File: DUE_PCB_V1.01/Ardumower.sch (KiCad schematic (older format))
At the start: 61 parts, among them J1 I2C_1, J10 Bumper Left, J11 Bumper Right, J12 P_Left, J13 P_Right, J14 Sonar_R, J15 Sonar_C, J16 Sonar_L, J17 US1, J18 US2, J19 US3, J2 I2C_2, J20 Button, J21 5V IN, J22 Remote, J23 PCB_2, J24 3.3V IN, J25 TX0/RX0, J26 TX1/RX1, J27 TX2/RX2, J28 GPS_TX/GPS_RX, J3 I2C_3, J4 DS3231 RTC, J5 9V IN, J6 Drop_Left, J7 Drop_Right, J8 Tilt, J9 Rain

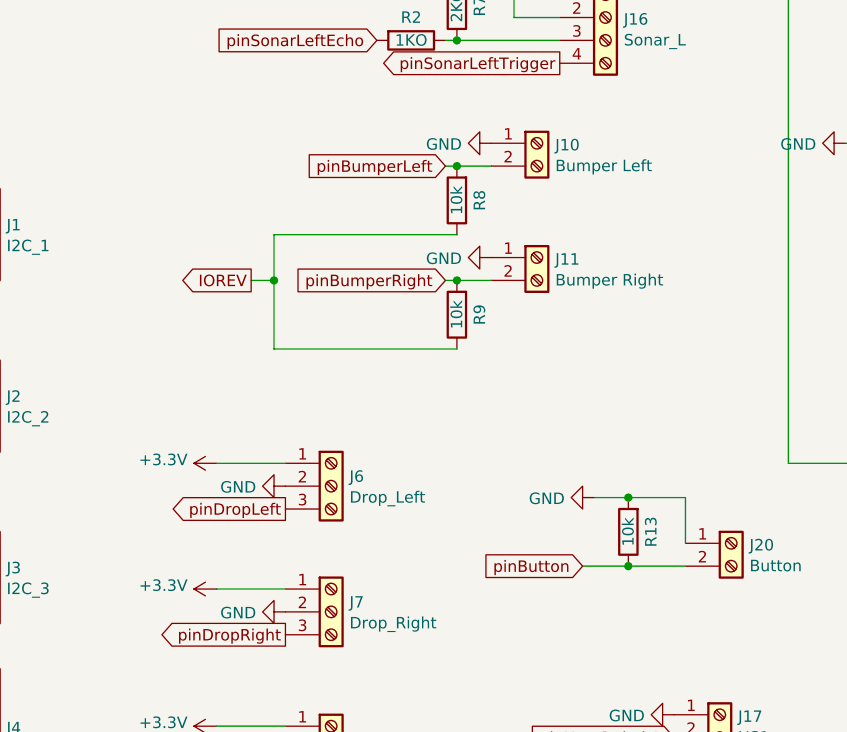
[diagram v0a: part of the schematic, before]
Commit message: Remove Resistors
Remove R8, R9 and R13
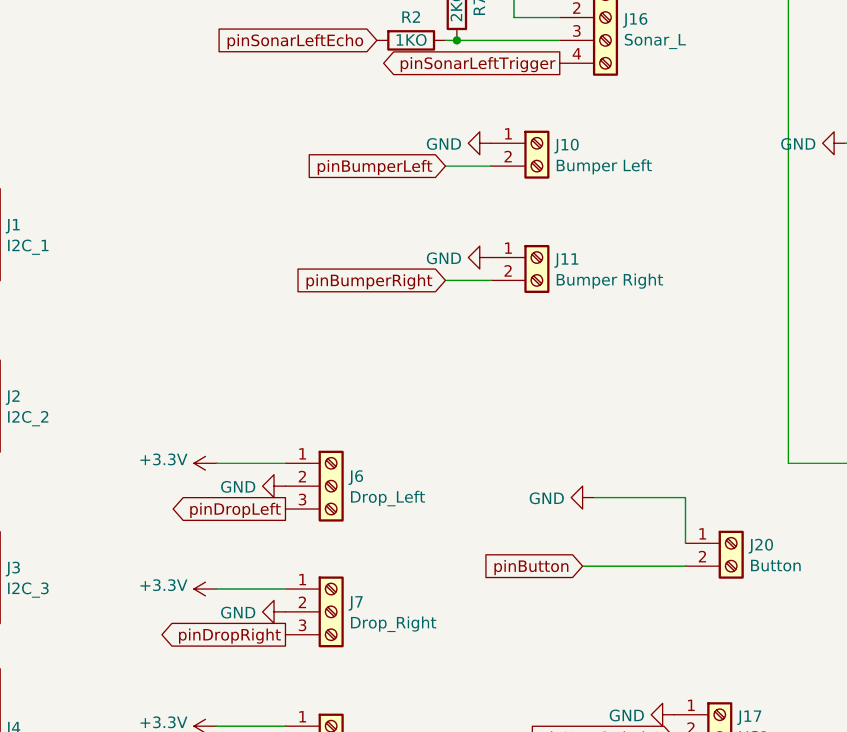
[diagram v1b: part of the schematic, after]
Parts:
- removed R13, R8, R9: 10k, Resistor_THT:R_Axial_DIN0207_L6.3mm_D2.5mm_P2.54mm_Vertical, symbol Device:R
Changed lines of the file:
@@
 ReservePinA10
 Wire Wire Line
-	2050 5000 2100 5000
-$Comp
-L Device:R R9
-U 1 1 6095136A
-P 2100 5150
-F 0 "R9" V 2000 5150 50  0000 C CNN
-F 1 "10k" V 2100 5150 50  0000 C CNN
-F 2 "Resistor_THT:R_Axial_DIN0207_L6.3mm_D2.5mm_P2.54mm_Vertical" V 2030 5150 50  0001 C CNN
-F 3 "~" H 2100 5150 50  0001 C CNN
-	1    2100 5150
-	-1   0    0    1
-$EndComp
-Connection ~ 2100 5000
-Wire Wire Line
-	2100 5000 2250 5000
-$Comp
-L Device:R R8
-U 1 1 6095AC18
-P 2100 4650
-F 0 "R8" V 2000 4650 50  0000 C CNN
-F 1 "10k" V 2100 4650 50  0000 C CNN
-F 2 "Resistor_THT:R_Axial_DIN0207_L6.3mm_D2.5mm_P2.54mm_Vertical" V 2030 4650 50  0001 C CNN
-F 3 "~" H 2100 4650 50  0001 C CNN
-	1    2100 4650
-	-1   0    0    1
-$EndComp
-Wire Wire Line
-	2050 4500 2100 4500
-Connection ~ 2100 4500
-Wire Wire Line
-	2100 4500 2250 4500
-Wire Wire Line
-	2100 4800 1300 4800
-Wire Wire Line
-	1300 4800 1300 5000
-Wire Wire Line
-	1300 5300 2100 5300
-Text GLabel 1200 5000 0    50   Output ~ 0
-IOREV
-Wire Wire Line
-	1200 5000 1300 5000
-Connection ~ 1300 5000
-Wire Wire Line
-	1300 5000 1300 5300
-Wire Wire Line
 	900  850  3550 850
-$Comp
-L Device:R R13
-U 1 1 60986E74
-P 2850 6100
-F 0 "R13" V 2750 6100 50  0000 C CNN
-F 1 "10k" V 2850 6100 50  0000 C CNN
-F 2 "Resistor_THT:R_Axial_DIN0207_L6.3mm_D2.5mm_P2.54mm_Vertical" V 2780 6100 50  0001 C CNN
-F 3 "~" H 2850 6100 50  0001 C CNN
-	1    2850 6100
-	-1   0    0    1
-$EndComp
-Wire Wire Line
-	2650 6250 2850 6250
-Connection ~ 2850 6250
-Wire Wire Line
-	2850 6250 3100 6250
-Wire Wire Line
-	2850 5950 2700 5950
 Wire Wire Line
 	10350 2400 10200 2400
@@
 $EndComp
 Wire Wire Line
-	2850 5950 3100 5950
-Wire Wire Line
 	3100 5950 3100 6150
-Connection ~ 2850 5950
 $Comp
 L Connector:Screw_Terminal_01x05 J25
@@
 	0    1    1    0
 $EndComp
+Wire Wire Line
+	2050 5000 2250 5000
+Wire Wire Line
+	2050 4500 2250 4500
+Wire Wire Line
+	2650 6250 3100 6250
+Wire Wire Line
+	2700 5950 3100 5950
 $EndSCHEMATC

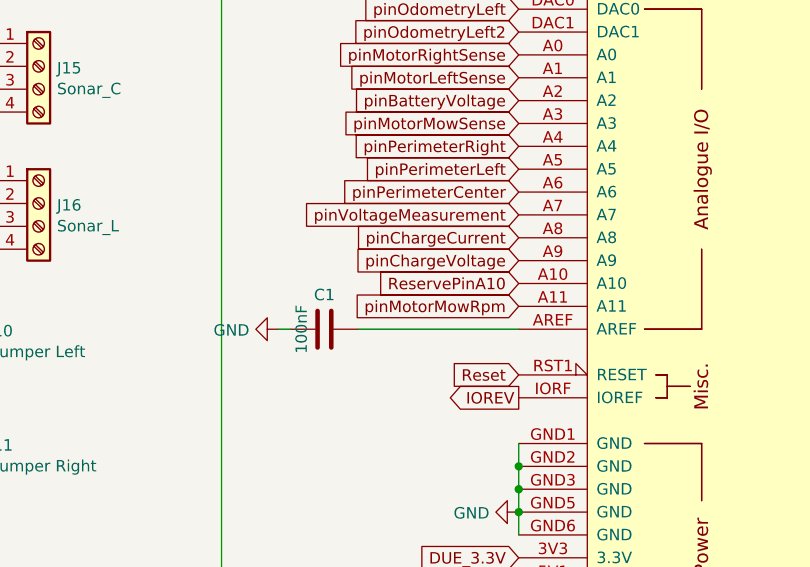
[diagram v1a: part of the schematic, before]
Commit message: Rename Pins
Rename ReservePinA10 to pinMotorLeftSense2
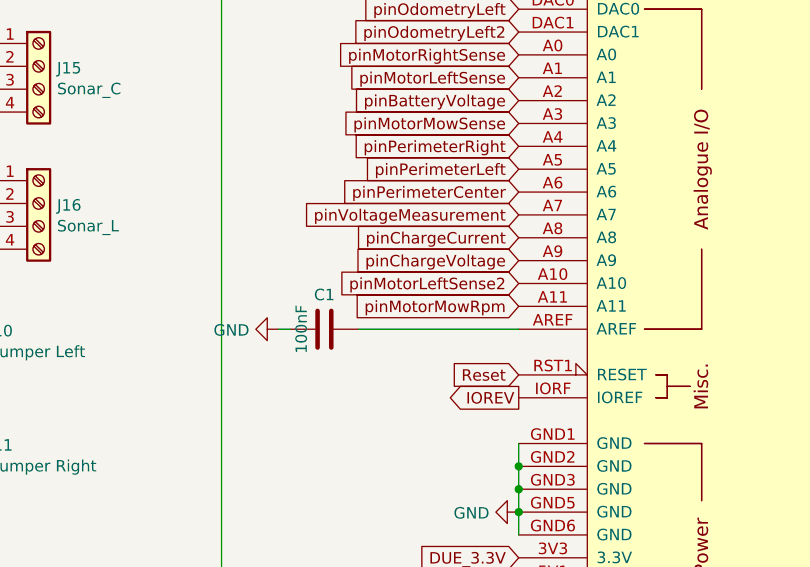
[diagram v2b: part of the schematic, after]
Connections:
- net ReservePinA10: no longer XA1.A10
- new net pinMotorLeftSense2: XA1.A10
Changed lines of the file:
@@
 ReservePinD49
 Text GLabel 4850 4200 0    50   Input ~ 0
-ReservePinA10
+pinMotorLeftSense2
 Text GLabel 9550 1300 0    50   Input ~ 0
 ReservePinA10

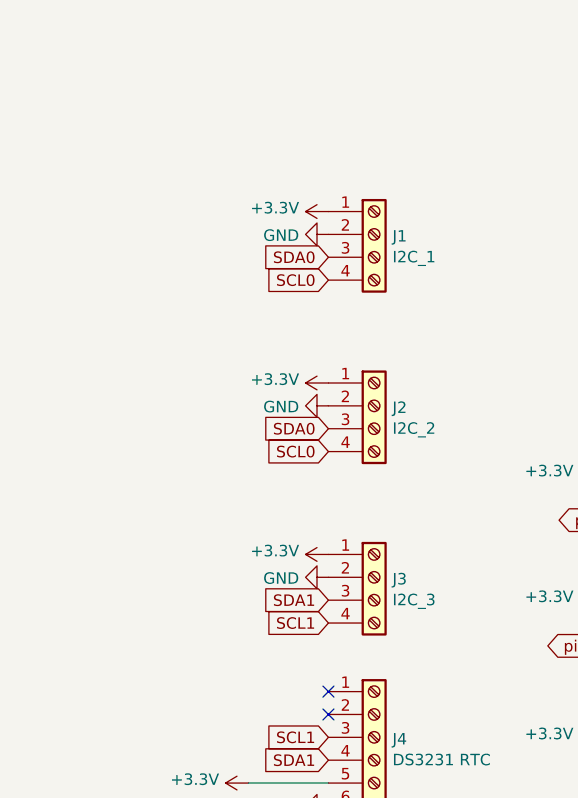
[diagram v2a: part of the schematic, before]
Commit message: Add I2C Pullup
Add i2c Pullup to J1 & J3
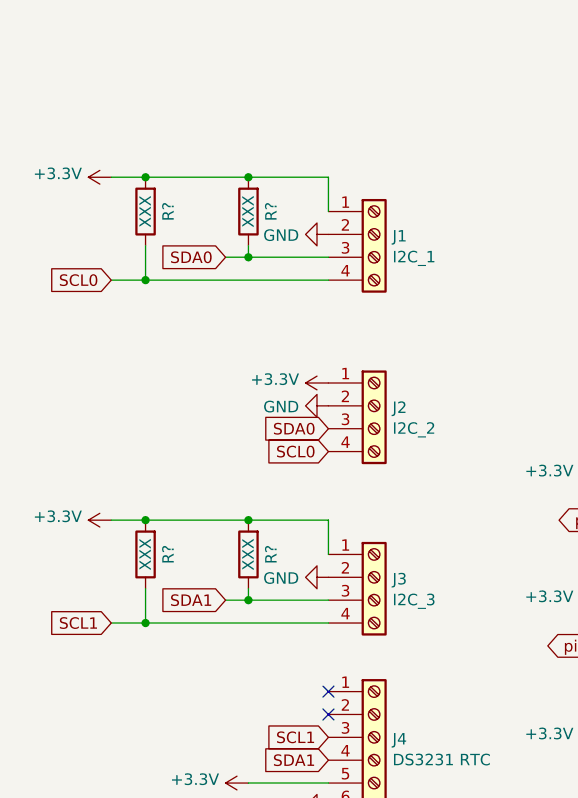
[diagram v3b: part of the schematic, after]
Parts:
- added R? (x4): XXX, Resistor_THT:R_Axial_DIN0207_L6.3mm_D2.5mm_P2.54mm_Vertical, symbol Device:R
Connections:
- net +3V3: now also R?.2, R?.2, R?.2, R?.2
- net SCL0: now also R?.1
- net SCL1: now also R?.1
- net SDA0: now also R?.1
- net SDA1: now also R?.1
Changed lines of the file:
@@
 Text GLabel 4850 2500 0    50   Input ~ 0
 SDA1
-Text GLabel -150 4850 0    50   Input ~ 0
+Text GLabel -600 4850 0    50   Input ~ 0
 SDA0
 Text GLabel -150 5600 0    50   Input ~ 0
 SDA0
-Text GLabel -150 6350 0    50   Input ~ 0
-SDA1
 Text GLabel 4850 2600 0    50   Input ~ 0
 SCL1
-Text GLabel -150 4950 0    50   Input ~ 0
+Text GLabel -1100 4950 0    50   Input ~ 0
 SCL0
 Text GLabel -150 5700 0    50   Input ~ 0
 SCL0
-Text GLabel -150 6450 0    50   Input ~ 0
-SCL1
 $Comp
 L Connector:Screw_Terminal_01x02 J5
@@
 $EndComp
 $Comp
-L power:GND #PWR07
-U 1 1 6097FEEB
-P -150 6250
-F 0 "#PWR07" H -150 6000 50  0001 C CNN
-F 1 "GND" V -145 6122 50  0000 R CNN
-F 2 "" H -150 6250 50  0001 C CNN
-F 3 "" H -150 6250 50  0001 C CNN
-	1    -150 6250
-	0    1    1    0
-$EndComp
-$Comp
 L power:GND #PWR05
 U 1 1 609801E6
@@
 L power:+3.3V #PWR02
 U 1 1 60A55674
-P -150 4650
-F 0 "#PWR02" H -150 4500 50  0001 C CNN
-F 1 "+3.3V" V -135 4778 50  0000 L CNN
-F 2 "" H -150 4650 50  0001 C CNN
-F 3 "" H -150 4650 50  0001 C CNN
-	1    -150 4650
+P -1100 4500
+F 0 "#PWR02" H -1100 4350 50  0001 C CNN
+F 1 "+3.3V" V -1085 4628 50  0000 L CNN
+F 2 "" H -1100 4500 50  0001 C CNN
+F 3 "" H -1100 4500 50  0001 C CNN
+	1    -1100 4500
 	0    -1   -1   0
 $EndComp
@@
 F 3 "" H -150 5400 50  0001 C CNN
 	1    -150 5400
-	0    -1   -1   0
-$EndComp
-$Comp
-L power:+3.3V #PWR06
-U 1 1 60A57F6D
-P -150 6150
-F 0 "#PWR06" H -150 6000 50  0001 C CNN
-F 1 "+3.3V" V -135 6278 50  0000 L CNN
-F 2 "" H -150 6150 50  0001 C CNN
-F 3 "" H -150 6150 50  0001 C CNN
-	1    -150 6150
 	0    -1   -1   0
 $EndComp
@@
 Wire Wire Line
 	2700 5950 3100 5950
+$Comp
+L Device:R R?
+U 1 1 609850CF
+P -950 4650
+F 0 "R?" V -1050 4650 50  0000 C CNN
+F 1 "XXX" V -950 4650 50  0000 C CNN
+F 2 "Resistor_THT:R_Axial_DIN0207_L6.3mm_D2.5mm_P2.54mm_Vertical" V -1020 4650 50  0001 C CNN
+F 3 "~" H -950 4650 50  0001 C CNN
+	1    -950 4650
+	-1   0    0    1
+$EndComp
+$Comp
+L Device:R R?
+U 1 1 6098F377
+P -500 4650
+F 0 "R?" V -600 4650 50  0000 C CNN
+F 1 "XXX" V -500 4650 50  0000 C CNN
+F 2 "Resistor_THT:R_Axial_DIN0207_L6.3mm_D2.5mm_P2.54mm_Vertical" V -570 4650 50  0001 C CNN
+F 3 "~" H -500 4650 50  0001 C CNN
+	1    -500 4650
+	-1   0    0    1
+$EndComp
+Wire Wire Line
+	-1100 4500 -950 4500
+Connection ~ -950 4500
+Wire Wire Line
+	-950 4500 -500 4500
+Wire Wire Line
+	-500 4500 -150 4500
+Wire Wire Line
+	-150 4500 -150 4650
+Connection ~ -500 4500
+Wire Wire Line
+	-600 4850 -500 4850
+Wire Wire Line
+	-500 4800 -500 4850
+Connection ~ -500 4850
+Wire Wire Line
+	-500 4850 -150 4850
+Wire Wire Line
+	-1100 4950 -950 4950
+Wire Wire Line
+	-950 4950 -950 4800
+Wire Wire Line
+	-950 4950 -150 4950
+Connection ~ -950 4950
+Text GLabel -600 6350 0    50   Input ~ 0
+SDA1
+Text GLabel -1100 6450 0    50   Input ~ 0
+SCL1
+$Comp
+L power:GND #PWR?
+U 1 1 609A6BE2
+P -150 6250
+F 0 "#PWR?" H -150 6000 50  0001 C CNN
+F 1 "GND" V -145 6122 50  0000 R CNN
+F 2 "" H -150 6250 50  0001 C CNN
+F 3 "" H -150 6250 50  0001 C CNN
+	1    -150 6250
+	0    1    1    0
+$EndComp
+$Comp
+L power:+3.3V #PWR?
+U 1 1 609A6BEC
+P -1100 6000
+F 0 "#PWR?" H -1100 5850 50  0001 C CNN
+F 1 "+3.3V" V -1085 6128 50  0000 L CNN
+F 2 "" H -1100 6000 50  0001 C CNN
+F 3 "" H -1100 6000 50  0001 C CNN
+	1    -1100 6000
+	0    -1   -1   0
+$EndComp
+$Comp
+L Device:R R?
+U 1 1 609A6BF6
+P -950 6150
+F 0 "R?" V -1050 6150 50  0000 C CNN
+F 1 "XXX" V -950 6150 50  0000 C CNN
+F 2 "Resistor_THT:R_Axial_DIN0207_L6.3mm_D2.5mm_P2.54mm_Vertical" V -1020 6150 50  0001 C CNN
+F 3 "~" H -950 6150 50  0001 C CNN
+	1    -950 6150
+	-1   0    0    1
+$EndComp
+$Comp
+L Device:R R?
+U 1 1 609A6C00
+P -500 6150
+F 0 "R?" V -600 6150 50  0000 C CNN
+F 1 "XXX" V -500 6150 50  0000 C CNN
+F 2 "Resistor_THT:R_Axial_DIN0207_L6.3mm_D2.5mm_P2.54mm_Vertical" V -570 6150 50  0001 C CNN
+F 3 "~" H -500 6150 50  0001 C CNN
+	1    -500 6150
+	-1   0    0    1
+$EndComp
+Wire Wire Line
+	-1100 6000 -950 6000
+Connection ~ -950 6000
+Wire Wire Line
+	-950 6000 -500 6000
+Wire Wire Line
+	-500 6000 -150 6000
+Connection ~ -500 6000
+Wire Wire Line
+	-600 6350 -500 6350
+Wire Wire Line
+	-500 6300 -500 6350
+Connection ~ -500 6350
+Wire Wire Line
+	-500 6350 -150 6350
+Wire Wire Line
+	-1100 6450 -950 6450
+Wire Wire Line
+	-950 6450 -950 6300
+Wire Wire Line
+	-950 6450 -150 6450
+Connection ~ -950 6450
+Wire Wire Line
+	-150 6000 -150 6150
 $EndSCHEMATC

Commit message: Update J30 and J32
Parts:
- gave numbers to parts that had none: 4
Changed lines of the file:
@@
 	2700 5950 3100 5950
 $Comp
-L Device:R R?
+L Device:R R8
 U 1 1 609850CF
 P -950 4650
-F 0 "R?" V -1050 4650 50  0000 C CNN
+F 0 "R8" V -1050 4650 50  0000 C CNN
 F 1 "XXX" V -950 4650 50  0000 C CNN
 F 2 "Resistor_THT:R_Axial_DIN0207_L6.3mm_D2.5mm_P2.54mm_Vertical" V -1020 4650 50  0001 C CNN
@@
 $EndComp
 $Comp
-L Device:R R?
+L Device:R R13
 U 1 1 6098F377
 P -500 4650
-F 0 "R?" V -600 4650 50  0000 C CNN
+F 0 "R13" V -600 4650 50  0000 C CNN
 F 1 "XXX" V -500 4650 50  0000 C CNN
 F 2 "Resistor_THT:R_Axial_DIN0207_L6.3mm_D2.5mm_P2.54mm_Vertical" V -570 4650 50  0001 C CNN
@@
 SCL1
 $Comp
-L power:GND #PWR?
+L power:GND #PWR07
 U 1 1 609A6BE2
 P -150 6250
-F 0 "#PWR?" H -150 6000 50  0001 C CNN
+F 0 "#PWR07" H -150 6000 50  0001 C CNN
 F 1 "GND" V -145 6122 50  0000 R CNN
 F 2 "" H -150 6250 50  0001 C CNN
@@
 $EndComp
 $Comp
-L power:+3.3V #PWR?
+L power:+3.3V #PWR06
 U 1 1 609A6BEC
 P -1100 6000
-F 0 "#PWR?" H -1100 5850 50  0001 C CNN
+F 0 "#PWR06" H -1100 5850 50  0001 C CNN
 F 1 "+3.3V" V -1085 6128 50  0000 L CNN
 F 2 "" H -1100 6000 50  0001 C CNN
@@
 $EndComp
 $Comp
-L Device:R R?
+L Device:R R9
 U 1 1 609A6BF6
 P -950 6150
-F 0 "R?" V -1050 6150 50  0000 C CNN
+F 0 "R9" V -1050 6150 50  0000 C CNN
 F 1 "XXX" V -950 6150 50  0000 C CNN
 F 2 "Resistor_THT:R_Axial_DIN0207_L6.3mm_D2.5mm_P2.54mm_Vertical" V -1020 6150 50  0001 C CNN
@@
 $EndComp
 $Comp
-L Device:R R?
+L Device:R R27
 U 1 1 609A6C00
 P -500 6150
-F 0 "R?" V -600 6150 50  0000 C CNN
+F 0 "R27" V -600 6150 50  0000 C CNN
 F 1 "XXX" V -500 6150 50  0000 C CNN
 F 2 "Resistor_THT:R_Axial_DIN0207_L6.3mm_D2.5mm_P2.54mm_Vertical" V -570 6150 50  0001 C CNN

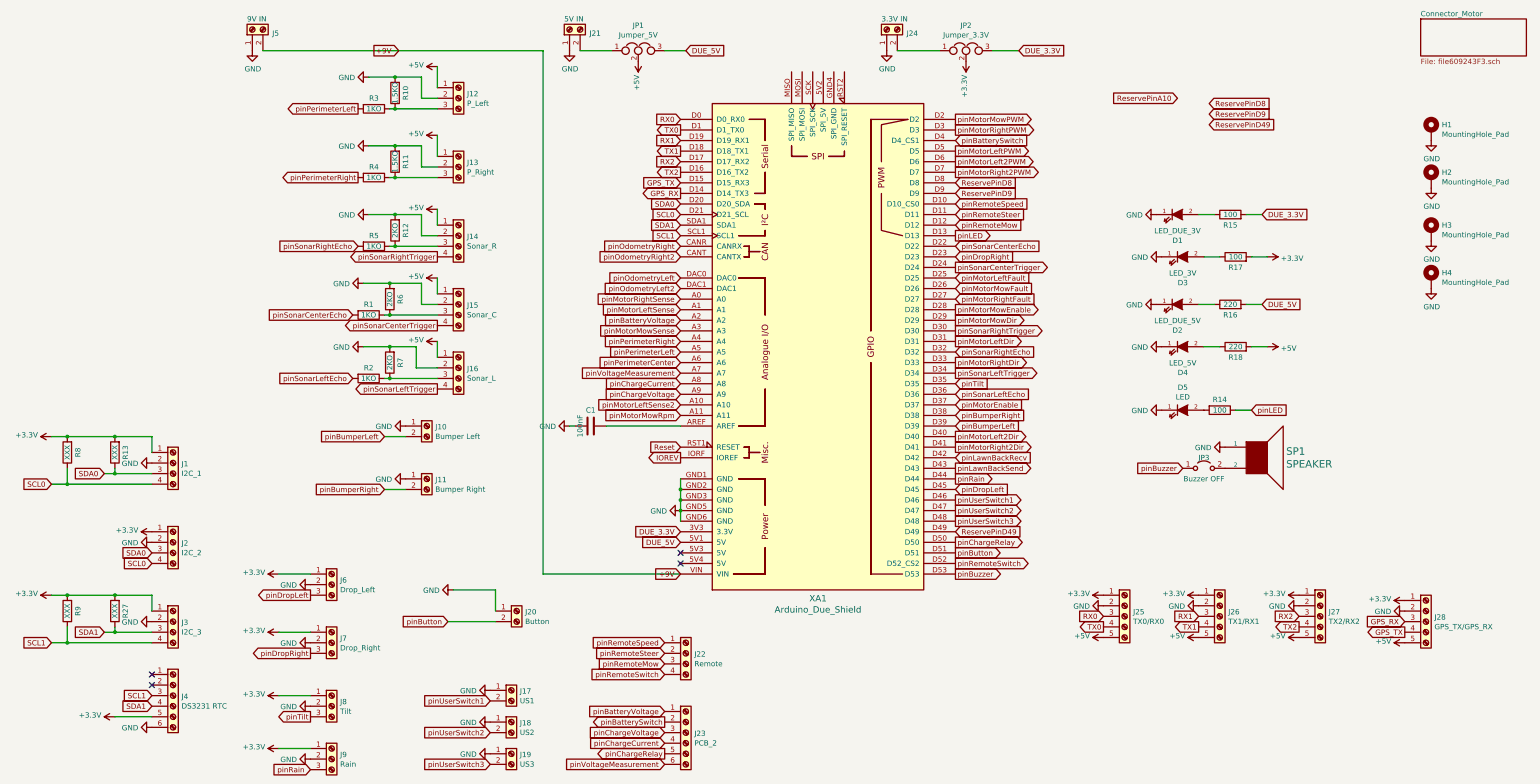
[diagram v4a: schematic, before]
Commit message: Start ro add Bernard changes from 1.02
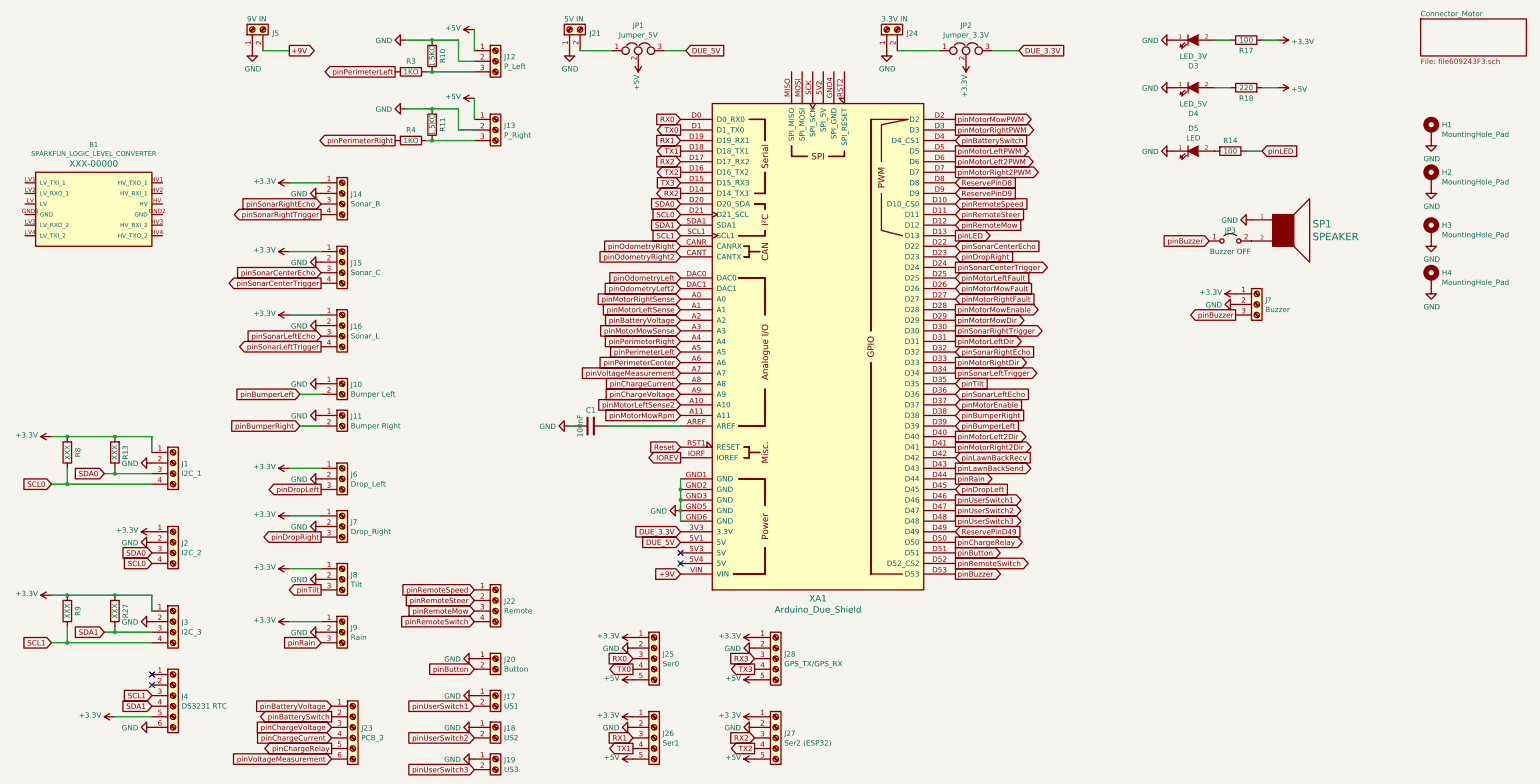
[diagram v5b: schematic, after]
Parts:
- removed D1: LED_DUE_3V, LED_THT:LED_D3.0mm, symbol Zimprich:LED
- removed D2: LED_DUE_5V, LED_THT:LED_D3.0mm, symbol Zimprich:LED
- removed R1, R2, R5: 1KO, Resistor_THT:R_Axial_DIN0207_L6.3mm_D2.5mm_P2.54mm_Vertical, symbol Device:R
- removed R12, R6, R7: 2KO, Resistor_THT:R_Axial_DIN0207_L6.3mm_D2.5mm_P2.54mm_Vertical, symbol Device:R
- removed R15: 100, Resistor_THT:R_Axial_DIN0207_L6.3mm_D2.5mm_P2.54mm_Vertical, symbol Device:R
- removed R16: 220, Resistor_THT:R_Axial_DIN0207_L6.3mm_D2.5mm_P2.54mm_Vertical, symbol Device:R
- added B1: SPARKFUN_LOGIC_LEVEL_CONVERTER, Boards:SPARKFUN_LOGIC_LEVEL_CONVERTER, symbol SparkFun-Boards:SPARKFUN_LOGIC_LEVEL_CONVERTER
- added J?: Buzzer, Connector_PinHeader_2.54mm:PinHeader_1x03_P2.54mm_Vertical, symbol Connector:Screw_Terminal_01x03
- J25: value TX0/RX0 -> Ser0
- J26: value TX1/RX1 -> Ser1
- J27: value TX2/RX2 -> Ser2 (ESP32)
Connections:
- net +3V3: now also J14.1 (Pin_1), J15.1 (Pin_1), J16.1 (Pin_1), J?.1 (Pin_1)
- net +5V: no longer J14.1 (Pin_1), J15.1 (Pin_1), J16.1 (Pin_1)
- net GND: now also J?.2 (Pin_2)
- net RX2: now also XA1.D14 (D14_TX3)
- net pinBuzzer: now also J?.3 (Pin_3)
- net pinSonarCenterEcho: now also J15.3 (Pin_3)
- net pinSonarLeftEcho: now also J16.3 (Pin_3)
- net pinSonarRightEcho: now also J14.3 (Pin_3)
- net GPS_RX renamed RX3
- net RX3: no longer XA1.D14 (D14_TX3)
- net GPS_TX renamed TX3
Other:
- moved on the sheet: D3, D4, D5, J10, J11, J12, J13, J14, J15, J16, J17, J18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

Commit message: Change I2C Names
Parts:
- removed J4: DS3231 RTC, Connector_PinHeader_2.54mm:PinHeader_1x06_P2.54mm_Vertical, symbol Connector:Screw_Terminal_01x06
- added J?: I2C1_2, Connector_PinHeader_2.54mm:PinHeader_1x04_P2.54mm_Vertical, symbol Connector:Screw_Terminal_01x04
- J1: value I2C_1 -> I2C0_1
- J2: value I2C_2 -> I2C0_2
- J3: value I2C_3 -> I2C1_1
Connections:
- net +3V3: now also J?.1 (Pin_1)
- net GND: now also J?.2 (Pin_2)
- net SCL1: now also J?.4 (Pin_4)
- net SDA1: now also J?.3 (Pin_3)
- no-connect marks 4 -> 2
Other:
- moved on the sheet: J1, J2, J3, R13, R27, R8, R9
